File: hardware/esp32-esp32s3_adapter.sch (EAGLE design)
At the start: 5 parts, among them U1 ESP32-S3-WROOM-1-N16R2, U2 ESP32-WROOM-32E_(16MB)

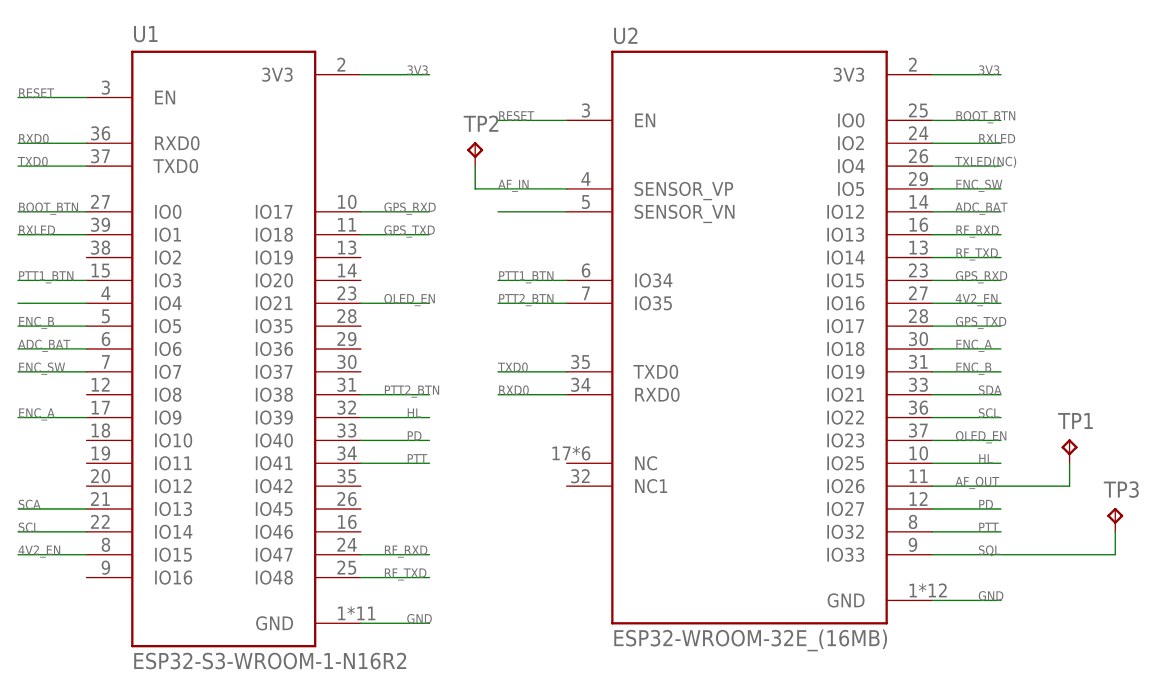
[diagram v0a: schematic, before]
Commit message: Added RevB of ESP32toESP32S3 V1.4 and 2.0
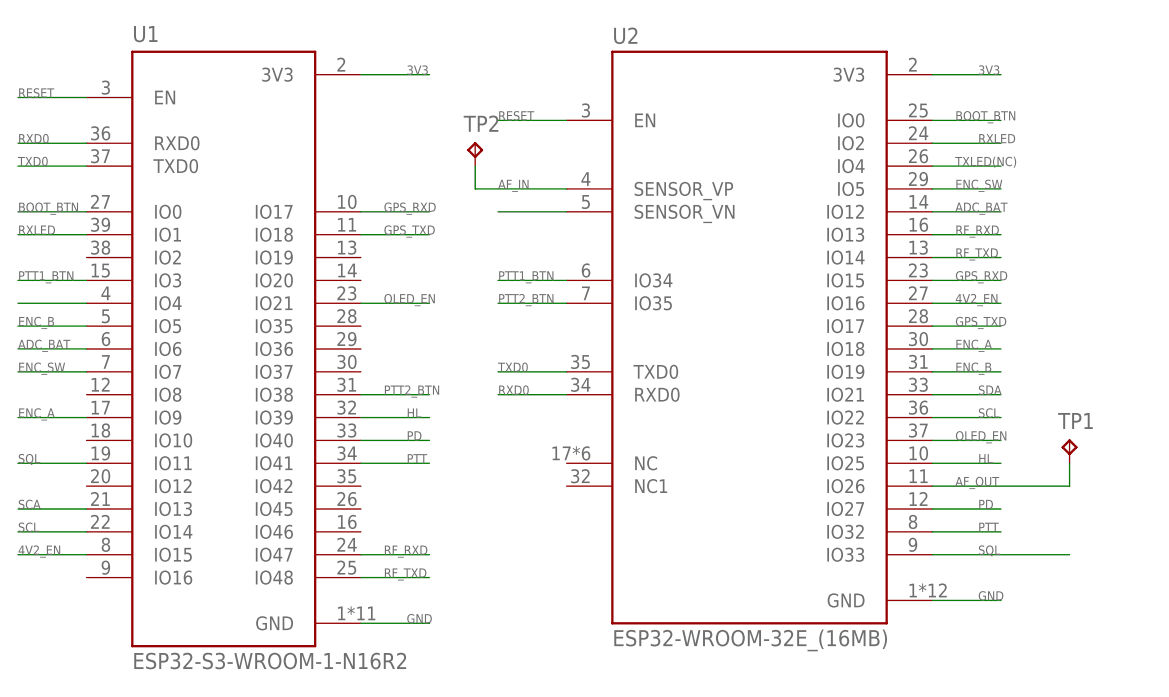
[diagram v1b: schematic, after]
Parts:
- removed TP3: TPB1,27, testpad:TPB1,27
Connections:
- net SQL: now also U1.IO11; no longer TP3.TP
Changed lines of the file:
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@@
 <part name="TP1" library="testpad" library_urn="urn:adsk.eagle:library:385" deviceset="TP" device="B1,27" package3d_urn="urn:adsk.eagle:package:27944/2" value="TPB1,27"/>
 <part name="TP2" library="testpad" library_urn="urn:adsk.eagle:library:385" deviceset="TP" device="B1,27" package3d_urn="urn:adsk.eagle:package:27944/2" value="TPB1,27"/>
-<part name="TP3" library="testpad" library_urn="urn:adsk.eagle:library:385" deviceset="TP" device="B1,27" package3d_urn="urn:adsk.eagle:package:27944/2" value="TPB1,27"/>
 </parts>
 <sheets>
@@
 <attribute name="TP_SIGNAL_NAME" x="54.61" y="69.85" size="1.778" layer="97"/>
 </instance>
-<instance part="TP3" gate="G$1" x="124.46" y="30.48" smashed="yes">
-<attribute name="NAME" x="123.19" y="31.75" size="1.778" layer="95"/>
-<attribute name="TP_SIGNAL_NAME" x="125.73" y="29.21" size="1.778" layer="97"/>
-</instance>
 </instances>
 <busses>
@@
 <pinref part="U2" gate="G$1" pin="IO33"/>
 <label x="109.22" y="25.4" size="1.016" layer="95"/>
-<wire x1="104.14" y1="25.4" x2="124.46" y2="25.4" width="0.1524" layer="91"/>
-<pinref part="TP3" gate="G$1" pin="TP"/>
-<wire x1="124.46" y1="25.4" x2="124.46" y2="27.94" width="0.1524" layer="91"/>
-</segment>
-</net>
+<wire x1="104.14" y1="25.4" x2="119.38" y2="25.4" width="0.1524" layer="91"/>
+</segment>
+<segment>
+<pinref part="U1" gate="G$1" pin="IO11"/>
+<wire x1="10.16" y1="35.56" x2="2.54" y2="35.56" width="0.1524" layer="91"/>
+<label x="2.54" y="35.56" size="1.016" layer="95"/>
+</segment>
+</net>

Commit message: RevC of ESP32-ESP32S3 Adapter SCH/PCB
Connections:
- removed net SCA: U1.IO13
- net SDA: now also U1.IO13
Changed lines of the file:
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@@
-</segment>
-</net>
-<net name="SCA" class="0">
-<segment>
-<pinref part="U1" gate="G$1" pin="IO13"/>
-<wire x1="10.16" y1="30.48" x2="2.54" y2="30.48" width="0.1524" layer="91"/>
-<label x="2.54" y="30.48" size="1.016" layer="95"/>
 </segment>
 </net>
@@
 <label x="109.22" y="43.18" size="1.016" layer="95"/>
 </segment>
+<segment>
+<pinref part="U1" gate="G$1" pin="IO13"/>
+<wire x1="10.16" y1="30.48" x2="2.54" y2="30.48" width="0.1524" layer="91"/>
+<label x="2.54" y="30.48" size="1.016" layer="95"/>
+</segment>
 </net>
